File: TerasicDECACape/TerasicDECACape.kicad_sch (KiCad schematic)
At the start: 35 parts, among them CN1 NASB0-S6701-TS50, CN2 NASB0-S6701-TS50, J1 MiSTer SDRAM Module, J2 USB_A, J3 Conn_01x03_Male, J4 Conn_02x05_Odd_Even, P8 BeagleBone_Black_Header, P9 BeagleBone_Black_Header, SW1 TS-1187A-B-A-B, SW2 TS-1187A-B-A-B

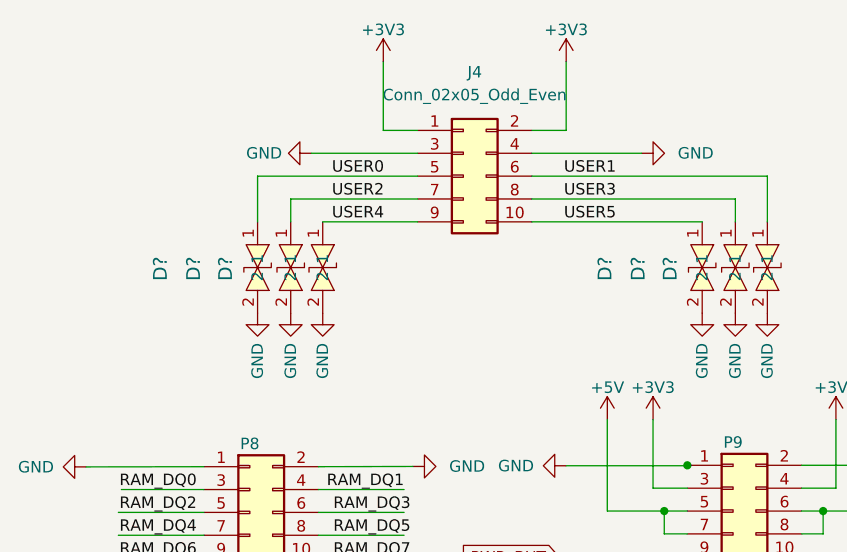
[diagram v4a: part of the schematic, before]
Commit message: add ESD to user header
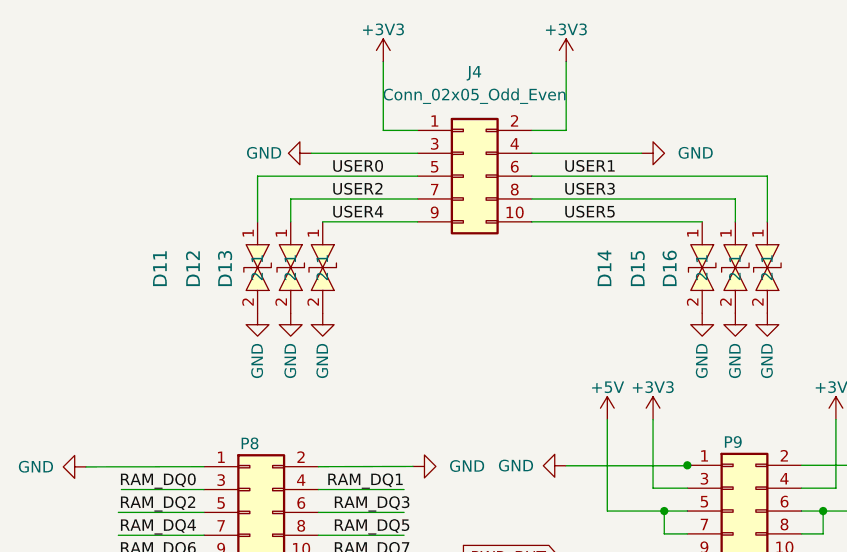
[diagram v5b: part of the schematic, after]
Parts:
- gave numbers to parts that had none: 6
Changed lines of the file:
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@@
   (symbol (lib_id "easyeda2kicad:LXES15AAA1-133") (at 97.536 48.641 270) (unit 1)
     (in_bom yes) (on_board yes)
-    (property "Reference" "D?" (id 0) (at 86.741 48.768 0)
+    (property "Reference" "D15" (id 0) (at 86.741 48.768 0)
       (effects (font (size 1.524 1.524)))
     )
@@
   (symbol (lib_id "power:GND") (at 101.092 53.721 0) (unit 1)
     (in_bom yes) (on_board yes) (fields_autoplaced)
-    (property "Reference" "#PWR?" (id 0) (at 101.092 60.071 0)
+    (property "Reference" "#PWR0134" (id 0) (at 101.092 60.071 0)
       (effects (font (size 1.27 1.27)) hide)
     )
@@
   (symbol (lib_id "power:GND") (at 93.853 53.721 0) (unit 1)
     (in_bom yes) (on_board yes) (fields_autoplaced)
-    (property "Reference" "#PWR?" (id 0) (at 93.853 60.071 0)
+    (property "Reference" "#PWR0133" (id 0) (at 93.853 60.071 0)
       (effects (font (size 1.27 1.27)) hide)
     )
@@
   (symbol (lib_id "easyeda2kicad:LXES15AAA1-133") (at 93.853 48.641 270) (unit 1)
     (in_bom yes) (on_board yes)
-    (property "Reference" "D?" (id 0) (at 83.058 48.768 0)
+    (property "Reference" "D14" (id 0) (at 83.058 48.768 0)
       (effects (font (size 1.524 1.524)))
     )
@@
   (symbol (lib_id "power:GND") (at 51.689 53.721 0) (unit 1)
     (in_bom yes) (on_board yes) (fields_autoplaced)
-    (property "Reference" "#PWR?" (id 0) (at 51.689 60.071 0)
+    (property "Reference" "#PWR0131" (id 0) (at 51.689 60.071 0)
       (effects (font (size 1.27 1.27)) hide)
     )
@@
   (symbol (lib_id "power:GND") (at 44.45 53.721 0) (unit 1)
     (in_bom yes) (on_board yes) (fields_autoplaced)
-    (property "Reference" "#PWR?" (id 0) (at 44.45 60.071 0)
+    (property "Reference" "#PWR0130" (id 0) (at 44.45 60.071 0)
       (effects (font (size 1.27 1.27)) hide)
     )
@@
   (symbol (lib_id "easyeda2kicad:LXES15AAA1-133") (at 48.133 48.641 270) (unit 1)
     (in_bom yes) (on_board yes)
-    (property "Reference" "D?" (id 0) (at 37.338 48.768 0)
+    (property "Reference" "D12" (id 0) (at 37.338 48.768 0)
       (effects (font (size 1.524 1.524)))
     )
@@
   (symbol (lib_id "easyeda2kicad:LXES15AAA1-133") (at 51.689 48.641 270) (unit 1)
     (in_bom yes) (on_board yes)
-    (property "Reference" "D?" (id 0) (at 40.894 48.768 0)
+    (property "Reference" "D13" (id 0) (at 40.894 48.768 0)
       (effects (font (size 1.524 1.524)))
     )
@@
   (symbol (lib_id "easyeda2kicad:LXES15AAA1-133") (at 101.092 48.641 270) (unit 1)
     (in_bom yes) (on_board yes)
-    (property "Reference" "D?" (id 0) (at 90.297 48.768 0)
+    (property "Reference" "D16" (id 0) (at 90.297 48.768 0)
       (effects (font (size 1.524 1.524)))
     )
@@
   (symbol (lib_id "power:GND") (at 97.536 53.721 0) (unit 1)
     (in_bom yes) (on_board yes) (fields_autoplaced)
-    (property "Reference" "#PWR?" (id 0) (at 97.536 60.071 0)
+    (property "Reference" "#PWR0135" (id 0) (at 97.536 60.071 0)
       (effects (font (size 1.27 1.27)) hide)
     )
@@
   (symbol (lib_id "power:GND") (at 48.133 53.721 0) (unit 1)
     (in_bom yes) (on_board yes) (fields_autoplaced)
-    (property "Reference" "#PWR?" (id 0) (at 48.133 60.071 0)
+    (property "Reference" "#PWR0132" (id 0) (at 48.133 60.071 0)
       (effects (font (size 1.27 1.27)) hide)
     )
@@
   (symbol (lib_id "easyeda2kicad:LXES15AAA1-133") (at 44.45 48.641 270) (unit 1)
     (in_bom yes) (on_board yes)
-    (property "Reference" "D?" (id 0) (at 33.655 48.768 0)
+    (property "Reference" "D11" (id 0) (at 33.655 48.768 0)
       (effects (font (size 1.524 1.524)))
     )
@@
       (reference "#PWR0129") (unit 1) (value "GND") (footprint "")
     )
+    (path "/5ffa540d-4eb2-4621-95c2-f225af79561b"
+      (reference "#PWR0130") (unit 1) (value "GND") (footprint "")
+    )
+    (path "/5b3f58df-1b1c-4fcd-844c-478b3aed2701"
+      (reference "#PWR0131") (unit 1) (value "GND") (footprint "")
+    )
+    (path "/d5b2b69f-34e7-4afe-80f6-b3552917c631"
+      (reference "#PWR0132") (unit 1) (value "GND") (footprint "")
+    )
+    (path "/37b1d238-71b9-4515-a097-a4424271069f"
+      (reference "#PWR0133") (unit 1) (value "GND") (footprint "")
+    )
     (path "/1b127cd0-60dc-4bc2-be10-80c32b073c51"
-      (reference "#PWR?") (unit 1) (value "GND") (footprint "")
-    )
-    (path "/37b1d238-71b9-4515-a097-a4424271069f"
-      (reference "#PWR?") (unit 1) (value "GND") (footprint "")
-    )
-    (path "/5b3f58df-1b1c-4fcd-844c-478b3aed2701"
-      (reference "#PWR?") (unit 1) (value "GND") (footprint "")
-    )
-    (path "/5ffa540d-4eb2-4621-95c2-f225af79561b"
-      (reference "#PWR?") (unit 1) (value "GND") (footprint "")
+      (reference "#PWR0134") (unit 1) (value "GND") (footprint "")
     )
     (path "/cab75a87-e198-49fd-a51a-ca3f8f244fd4"
-      (reference "#PWR?") (unit 1) (value "GND") (footprint "")
-    )
-    (path "/d5b2b69f-34e7-4afe-80f6-b3552917c631"
-      (reference "#PWR?") (unit 1) (value "GND") (footprint "")
+      (reference "#PWR0135") (unit 1) (value "GND") (footprint "")
     )
     (path "/351874dc-99f1-41fb-8357-28151f7d437e"
@@
       (reference "D10") (unit 1) (value "red") (footprint "LED_SMD:LED_0603_1608Metric")
     )
+    (path "/d5c16ce1-302b-44c1-b6a0-7d08a3c2217a"
+      (reference "D11") (unit 1) (value "LXES15AAA1-133") (footprint "D0402-BI")
+    )
+    (path "/6bb0d1c6-1d6b-4fe5-a624-457022ac2147"
+      (reference "D12") (unit 1) (value "LXES15AAA1-133") (footprint "D0402-BI")
+    )
+    (path "/6dedb8f7-4151-4be2-a231-9daeebdd5684"
+      (reference "D13") (unit 1) (value "LXES15AAA1-133") (footprint "D0402-BI")
+    )
+    (path "/49a8c814-d4e4-4072-abfb-9a34070c3de2"
+      (reference "D14") (unit 1) (value "LXES15AAA1-133") (footprint "D0402-BI")
+    )
     (path "/1537df2b-d5b6-4258-a0c8-b09fa5be3e6b"
-      (reference "D?") (unit 1) (value "LXES15AAA1-133") (footprint "D0402-BI")
-    )
-    (path "/49a8c814-d4e4-4072-abfb-9a34070c3de2"
-      (reference "D?") (unit 1) (value "LXES15AAA1-133") (footprint "D0402-BI")
-    )
-    (path "/6bb0d1c6-1d6b-4fe5-a624-457022ac2147"
-      (reference "D?") (unit 1) (value "LXES15AAA1-133") (footprint "D0402-BI")
-    )
-    (path "/6dedb8f7-4151-4be2-a231-9daeebdd5684"
-      (reference "D?") (unit 1) (value "LXES15AAA1-133") (footprint "D0402-BI")
+      (reference "D15") (unit 1) (value "LXES15AAA1-133") (footprint "D0402-BI")
     )
     (path "/aafd2f27-7c7d-4ecc-8bc5-f01a85d2921b"
-      (reference "D?") (unit 1) (value "LXES15AAA1-133") (footprint "D0402-BI")
-    )
-    (path "/d5c16ce1-302b-44c1-b6a0-7d08a3c2217a"
-      (reference "D?") (unit 1) (value "LXES15AAA1-133") (footprint "D0402-BI")
+      (reference "D16") (unit 1) (value "LXES15AAA1-133") (footprint "D0402-BI")
     )
     (path "/dee682ae-5831-4458-aee8-f10821032dc7"

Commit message: schematic and PCB cosmetics
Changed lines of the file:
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@@
+    (stroke (width 0) (type default) (color 0 0 0 0))
+  )
+  (wire (pts (xy 104.902 106.172) (xy 120.523 106.172))
     (stroke (width 0) (type default) (color 0 0 0 0))
   )
@@
     (stroke (width 0) (type default) (color 0 0 0 0))
   )
+  (wire (pts (xy 104.902 103.632) (xy 120.523 103.632))
+    (stroke (width 0) (type default) (color 0 0 0 0))
+  )
   (wire (pts (xy 118.618 83.312) (xy 104.902 83.312))
     (stroke (width 0) (type default) (color 0 0 0 0))
@@
     (stroke (width 0) (type default) (color 0 0 0 0))
   )
-  (wire (pts (xy 118.618 106.172) (xy 104.902 106.172))
-    (stroke (width 0) (type default) (color 0 0 0 0))
-  )
   (wire (pts (xy 250.19 90.932) (xy 263.906 90.932))
     (stroke (width 0) (type default) (color 0 0 0 0))
@@
     (stroke (width 0) (type default) (color 0 0 0 0))
   )
-  (wire (pts (xy 118.618 103.632) (xy 104.902 103.632))
-    (stroke (width 0) (type default) (color 0 0 0 0))
-  )
   (wire (pts (xy 38.5064 116.4844) (xy 28.9814 116.4844))
     (stroke (width 0) (type default) (color 0 0 0 0))
@@
     (effects (font (size 1.27 1.27)) (justify left bottom))
   )
-  (label "PG8_UART1_RTS" (at 118.618 106.172 180)
+  (label "PG8_UART1_RTS" (at 120.523 106.172 180)
     (effects (font (size 1.27 1.27)) (justify right bottom))
   )
@@
     (effects (font (size 1.27 1.27)) (justify left bottom))
   )
-  (label "PG9_UART1_CTS" (at 118.618 103.632 180)
-    (effects (font (size 1.27 1.27)) (justify right bottom))
-  )
+  (label "PG9_UART1_CTS" (at 120.523 103.632 180)
+    (effects (font (size 1.27 1.27)) (justify right bottom))
+  )

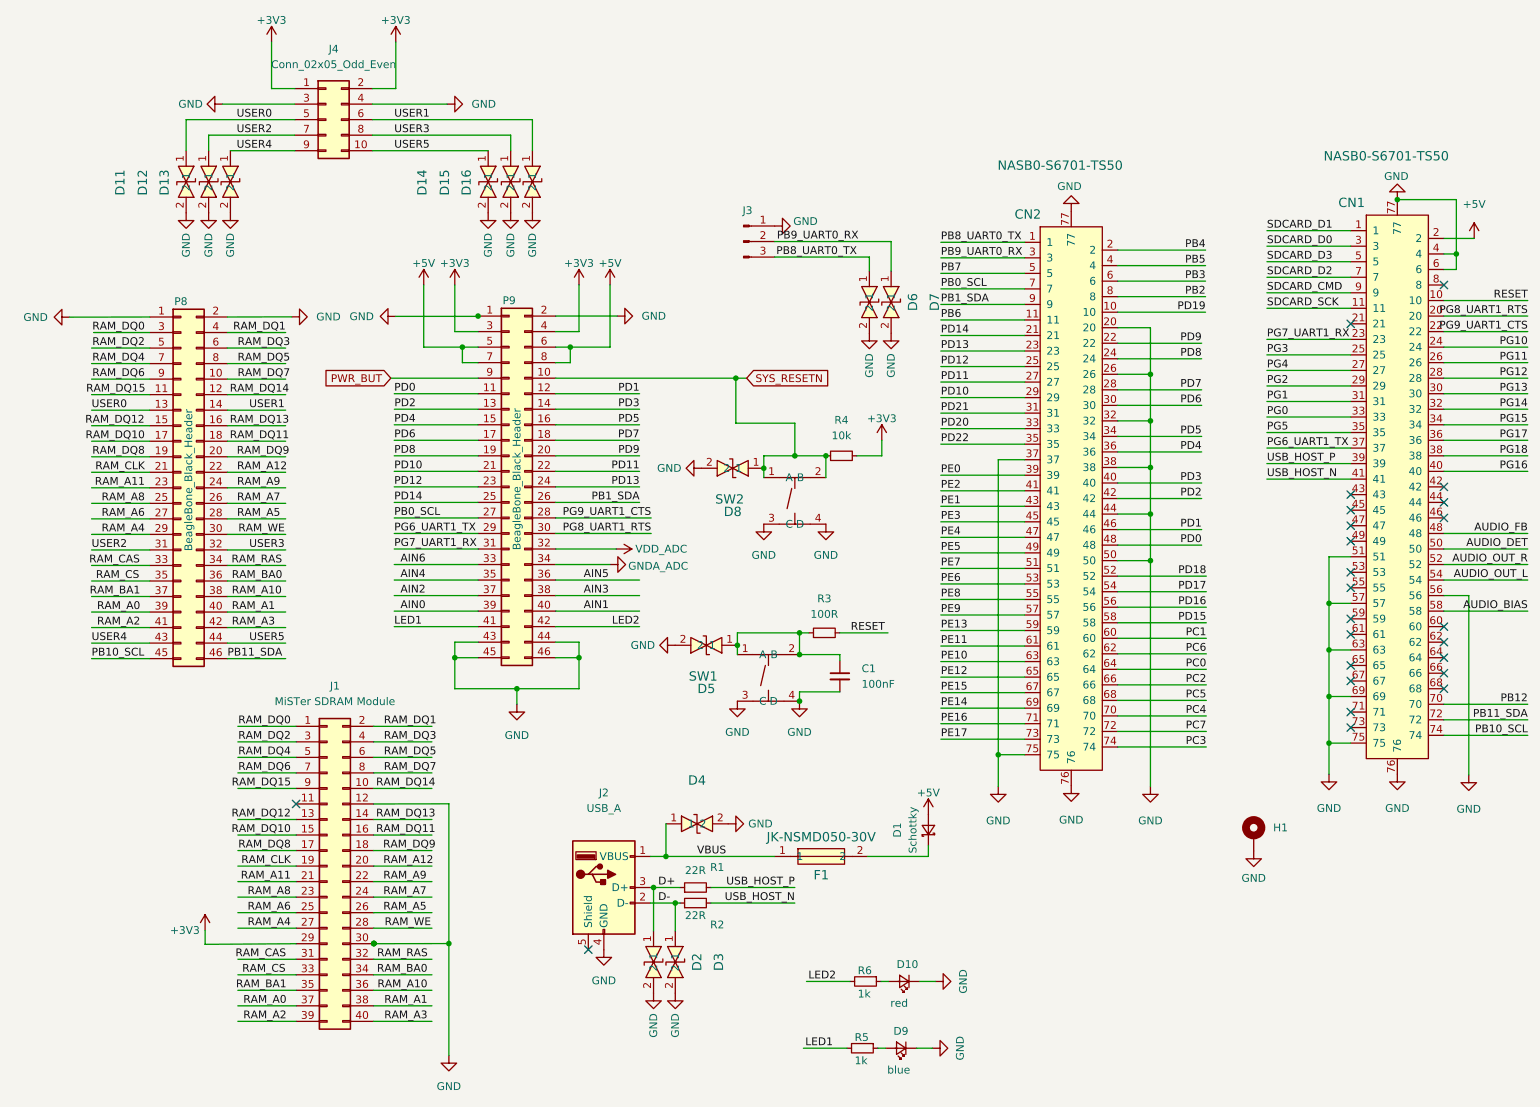
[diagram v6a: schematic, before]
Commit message: remove LEDs, because we have enough on the base board, add their pins to USER IO
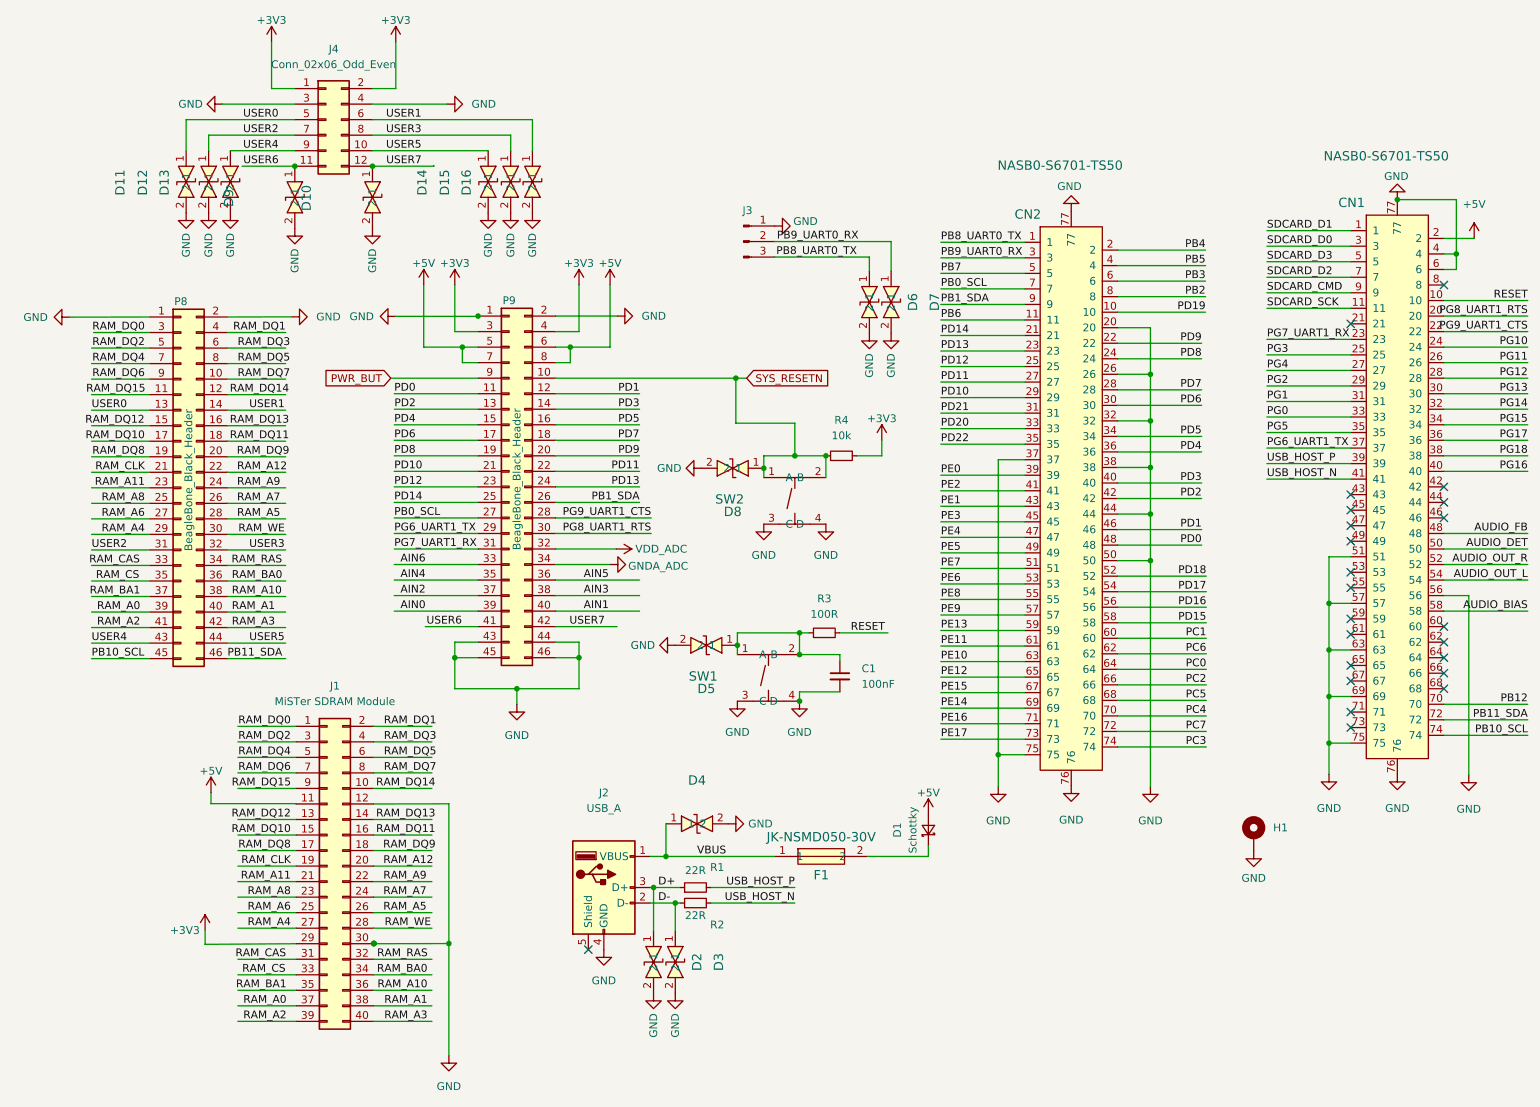
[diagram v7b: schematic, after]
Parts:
- removed D10: red, LED_SMD:LED_0603_1608Metric, symbol Device:LED_Small
- removed D9: blue, LED_SMD:LED_0603_1608Metric, symbol Device:LED_Small
- removed J4: Conn_02x05_Odd_Even, Connector_PinSocket_2.54mm:PinSocket_2x05_P2.54mm_Vertical, symbol Connector_Generic:Conn_02x05_Odd_Even
- removed R5, R6: 1k, Resistor_SMD:R_0603_1608Metric, symbol Device:R_Small
- added D10, D9: LXES15AAA1-133, D0402-BI, symbol easyeda2kicad:LXES15AAA1-133
- added J4: Conn_02x06_Odd_Even, Connector_PinSocket_2.54mm:PinSocket_2x06_P2.54mm_Vertical, symbol Connector_Generic:Conn_02x06_Odd_Even
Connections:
- net +3V3: now also J4.1 (Pin_1), J4.2 (Pin_2)
- net +5V: now also J1.11 (Pin_11)
- net GND: now also D10.2, D9.2, J4.3 (Pin_3), J4.4 (Pin_4)
- net USER0: now also J4.5 (Pin_5)
- net USER1: now also J4.6 (Pin_6)
- net USER2: now also J4.7 (Pin_7)
- net USER3: now also J4.8 (Pin_8)
- net USER4: now also J4.9 (Pin_9)
- net USER5: now also J4.10 (Pin_10)
- net LED1 renamed USER6
- net USER6: now also D9.1, J4.11 (Pin_11)
- net LED2 renamed USER7
- net USER7: now also D10.1, J4.12 (Pin_12)
- no-connect marks 24 -> 23
